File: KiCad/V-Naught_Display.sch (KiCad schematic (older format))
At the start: 22 parts, among them J1 USB_B_Micro, J2 I2C Header, J3 Conn_01x03, J4 Conn_01x02, SW1 SW_SPST, SW2 SW_SPST, SW3 SW_SPST, SW4 SW_SPST, SW5 SW_SPST, U1 AP2127K-3.3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

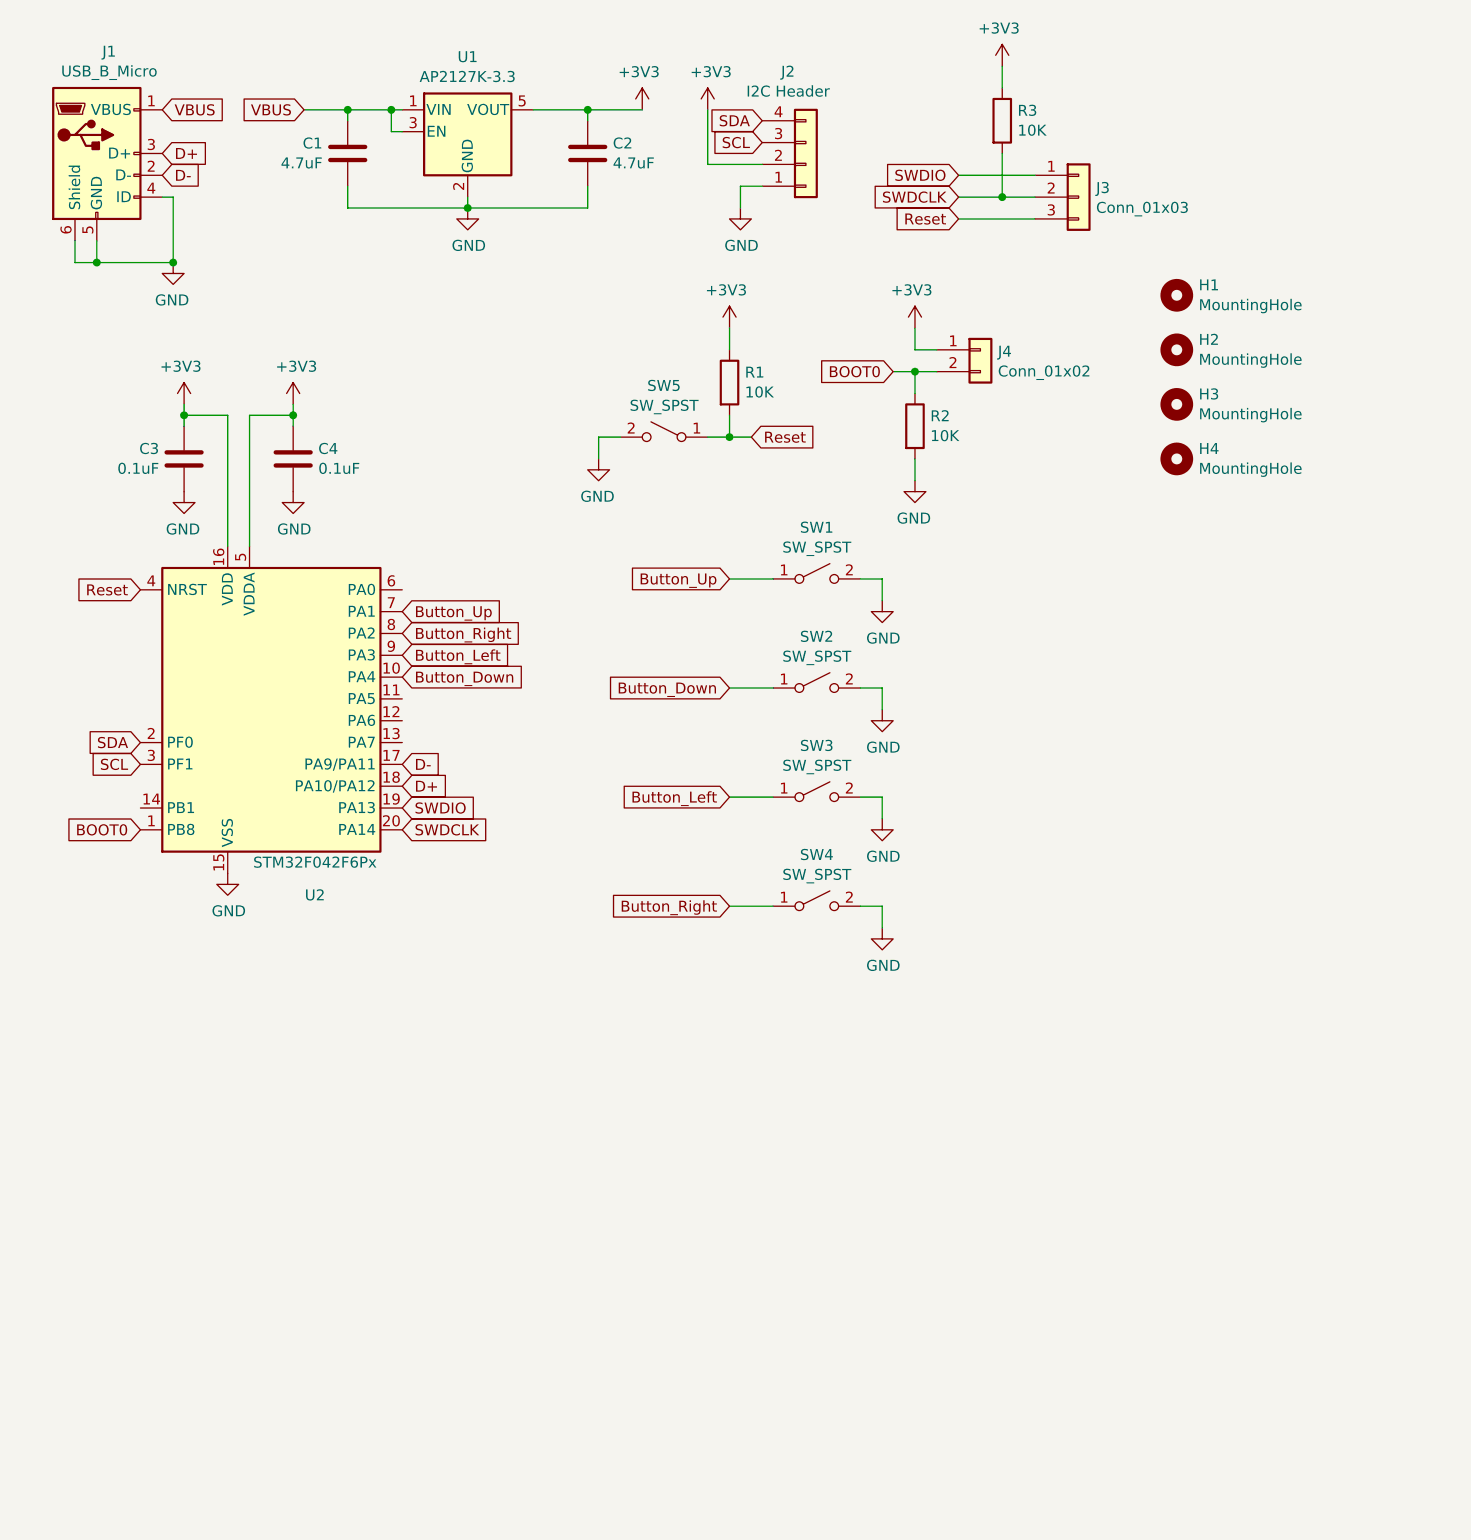
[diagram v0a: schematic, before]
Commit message: Production File updates
Added a click encoder to the center of the buttons as an additional option for input instead of discrete buttons.

Klipper Config will follow with pinmaps when the boards arrive.
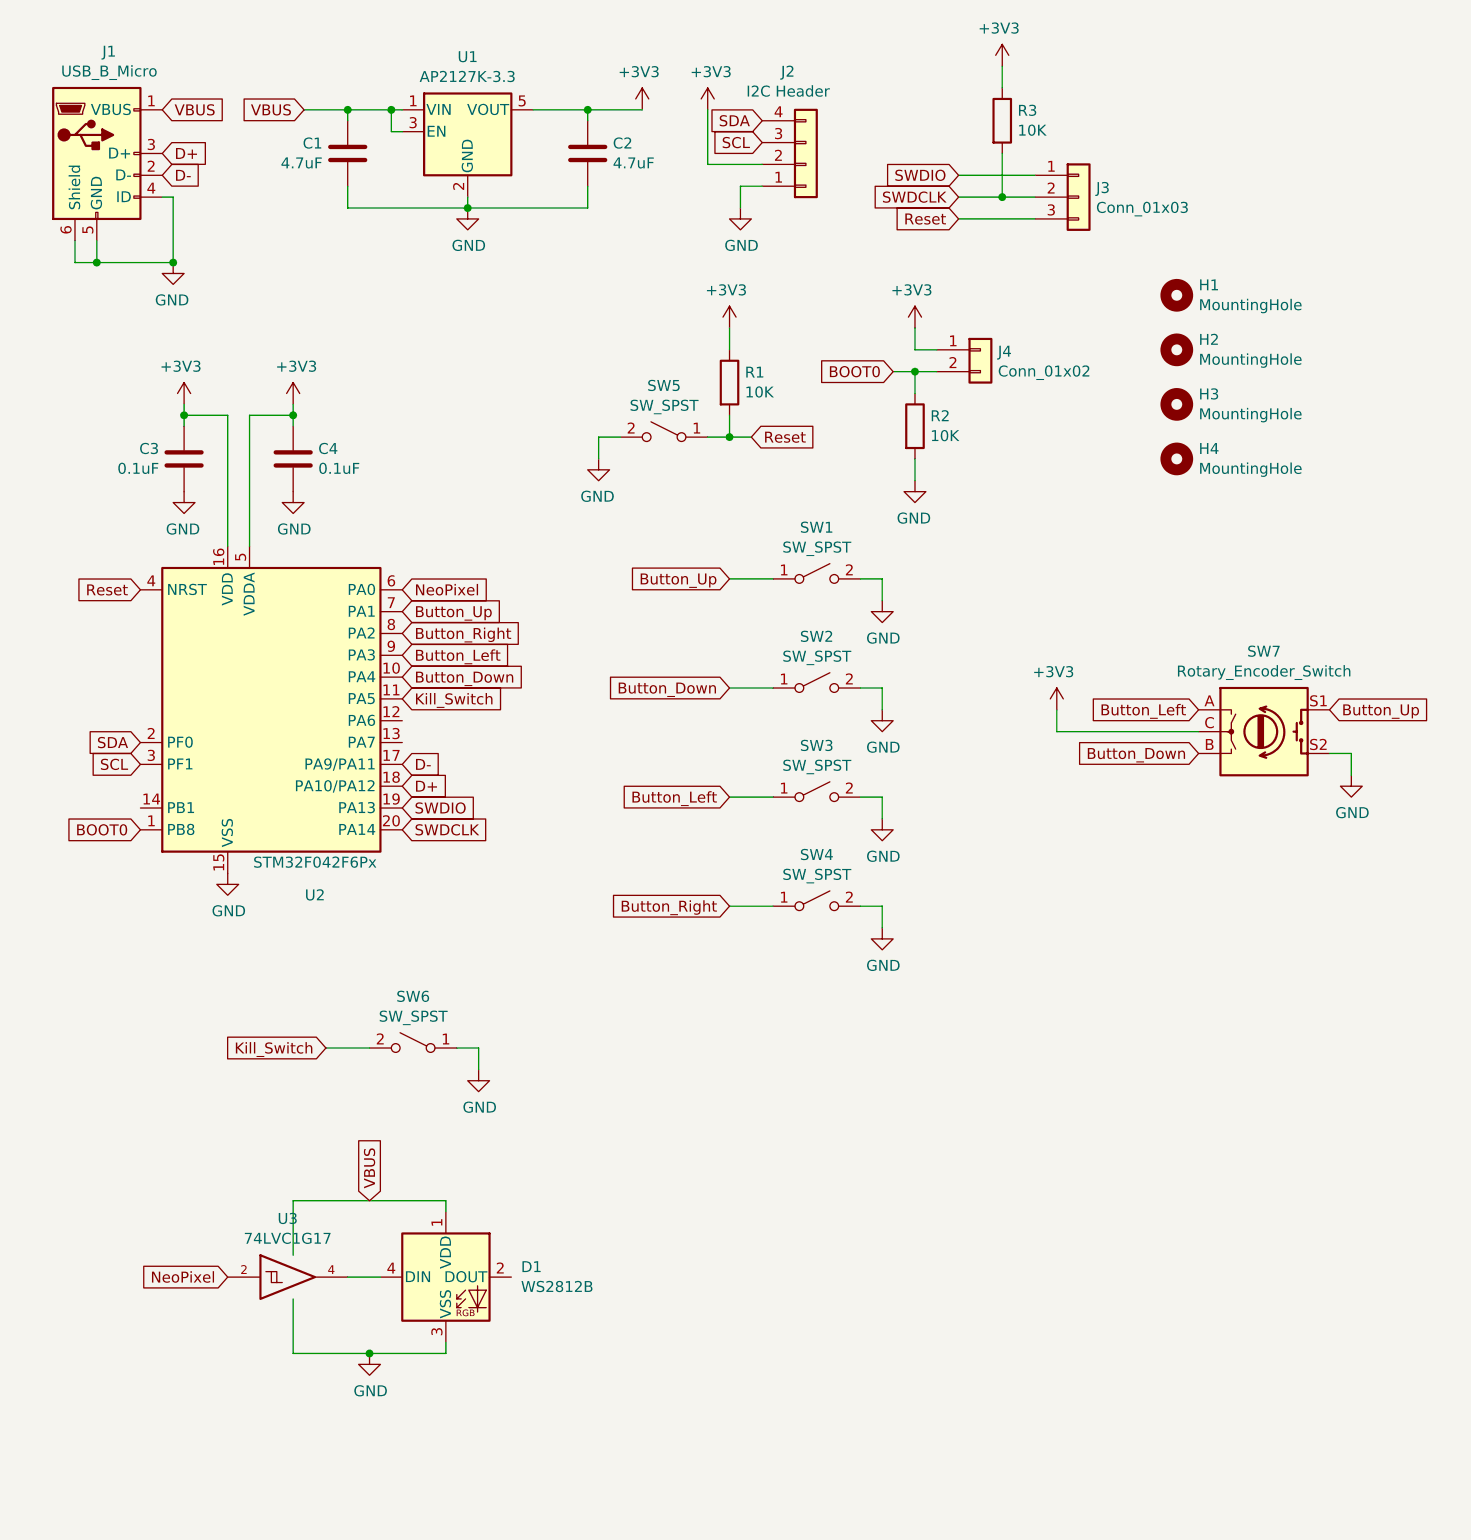
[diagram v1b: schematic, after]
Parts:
- added D1: WS2812B, LED_SMD:LED_WS2812B_PLCC4_5.0x5.0mm_P3.2mm, symbol LED:WS2812B
- added SW6: SW_SPST, Button_Switch_THT:SW_PUSH_6mm, symbol Switch:SW_SPST
- added SW7: Rotary_Encoder_Switch, TRA_KiCad_Footprints:EN11 Encoder, symbol Device:Rotary_Encoder_Switch
- added U3: 74LVC1G17, Package_TO_SOT_SMD:SOT-353_SC-70-5, symbol 74xGxx:74LVC1G17
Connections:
- net +3V3: now also SW7.C
- net Button_Down: now also SW7.B
- net Button_Left: now also SW7.A
- net Button_Up: now also SW7.S1
- net GND: now also D1.3 (VSS), SW6.1 (A), SW7.S2, U3.3 (GND)
- net Kill_Switch: now reaches U2.11 (PA5)
- net Kill_Switch: now also SW6.2 (B)
- net NeoPixel: now reaches U2.6 (PA0)
- net NeoPixel: now also U3.2
- net VBUS renamed VCC
- net VCC: now also D1.1 (VDD), U3.5 (VCC)
- new net: D1.4 (DIN), U3.4
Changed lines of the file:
@@
 	1    0    0    1
 $EndComp
+Text GLabel 1950 5250 0    50   Input ~ 0
+Kill_Switch
+$Comp
+L power:GND #PWR0120
+U 1 1 5E225054
+P 2650 5350
+F 0 "#PWR0120" H 2650 5100 50  0001 C CNN
+F 1 "GND" H 2655 5177 50  0000 C CNN
+F 2 "" H 2650 5350 50  0001 C CNN
+F 3 "" H 2650 5350 50  0001 C CNN
+	1    2650 5350
+	1    0    0    -1
+$EndComp
+Wire Wire Line
+	2650 5350 2650 5250
+Wire Wire Line
+	2650 5250 2550 5250
+Wire Wire Line
+	2150 5250 1950 5250
+Text GLabel 2300 3650 2    50   Input ~ 0
+Kill_Switch
+$Comp
+L 74xGxx:74LVC1G17 U3
+U 1 1 5E22767C
+P 1800 6300
+F 0 "U3" H 1775 6567 50  0000 C CNN
+F 1 "74LVC1G17" H 1775 6476 50  0000 C CNN
+F 2 "Package_TO_SOT_SMD:SOT-353_SC-70-5" H 1800 6300 50  0001 C CNN
+F 3 "http://www.ti.com/lit/sg/scyt129e/scyt129e.pdf" H 1800 6300 50  0001 C CNN
+	1    1800 6300
+	1    0    0    -1
+$EndComp
+Text GLabel 2150 5950 1    50   Input ~ 0
+VBUS
+$Comp
+L LED:WS2812B D1
+U 1 1 5E22982F
+P 2500 6300
+F 0 "D1" H 2844 6346 50  0000 L CNN
+F 1 "WS2812B" H 2844 6255 50  0000 L CNN
+F 2 "LED_SMD:LED_WS2812B_PLCC4_5.0x5.0mm_P3.2mm" H 2550 6000 50  0001 L TNN
+F 3 "https://cdn-shop.adafruit.com/datasheets/WS2812B.pdf" H 2600 5925 50  0001 L TNN
+	1    2500 6300
+	1    0    0    -1
+$EndComp
+Wire Wire Line
+	2500 6000 2500 5950
+Wire Wire Line
+	2500 5950 1800 5950
+Wire Wire Line
+	1800 5950 1800 6200
+Wire Wire Line
+	1800 6400 1800 6650
+Wire Wire Line
+	1800 6650 2150 6650
+Wire Wire Line
+	2500 6650 2500 6600
+Wire Wire Line
+	2200 6300 2050 6300
+$Comp
+L power:GND #PWR0121
+U 1 1 5E23384D
+P 2150 6650
+F 0 "#PWR0121" H 2150 6400 50  0001 C CNN
+F 1 "GND" H 2155 6477 50  0000 C CNN
+F 2 "" H 2150 6650 50  0001 C CNN
+F 3 "" H 2150 6650 50  0001 C CNN
+	1    2150 6650
+	1    0    0    -1
+$EndComp
+Text GLabel 1500 6300 0    50   Input ~ 0
+NeoPixel
+Text GLabel 2300 3150 2    50   Input ~ 0
+NeoPixel
+Connection ~ 2150 6650
+Wire Wire Line
+	2150 6650 2500 6650
+$Comp
+L Device:Rotary_Encoder_Switch SW7
+U 1 1 5E23C835
+P 6250 3800
+F 0 "SW7" H 6250 4167 50  0000 C CNN
+F 1 "Rotary_Encoder_Switch" H 6250 4076 50  0000 C CNN
+F 2 "TRA_KiCad_Footprints:EN11 Encoder" H 6100 3960 50  0001 C CNN
+F 3 "~" H 6250 4060 50  0001 C CNN
+	1    6250 3800
+	1    0    0    -1
+$EndComp
+Text GLabel 6550 3700 2    50   Input ~ 0
+Button_Up
+Text GLabel 5950 3900 0    50   Input ~ 0
+Button_Down
+Text GLabel 5950 3700 0    50   Input ~ 0
+Button_Left
+$Comp
+L power:GND #PWR0122
+U 1 1 5E2449F3
+P 6650 4000
+F 0 "#PWR0122" H 6650 3750 50  0001 C CNN
+F 1 "GND" H 6655 3827 50  0000 C CNN
+F 2 "" H 6650 4000 50  0001 C CNN
+F 3 "" H 6650 4000 50  0001 C CNN
+	1    6650 4000
+	1    0    0    -1
+$EndComp
+Wire Wire Line
+	6650 4000 6650 3900
+Wire Wire Line
+	6650 3900 6550 3900
+Wire Wire Line
+	5950 3800 5300 3800
+Wire Wire Line
+	5300 3800 5300 3700
+$Comp
+L power:+3V3 #PWR0123
+U 1 1 5E248221
+P 5300 3700
+F 0 "#PWR0123" H 5300 3550 50  0001 C CNN
+F 1 "+3V3" H 5315 3873 50  0000 C CNN
+F 2 "" H 5300 3700 50  0001 C CNN
+F 3 "" H 5300 3700 50  0001 C CNN
+	1    5300 3700
+	-1   0    0    -1
+$EndComp
+$Comp
+L Switch:SW_SPST SW6
+U 1 1 5E24B6BA
+P 2350 5250
+F 0 "SW6" H 2350 5485 50  0000 C CNN
+F 1 "SW_SPST" H 2350 5394 50  0000 C CNN
+F 2 "Button_Switch_THT:SW_PUSH_6mm" H 2350 5250 50  0001 C CNN
+F 3 "~" H 2350 5250 50  0001 C CNN
+	1    2350 5250
+	-1   0    0    -1
+$EndComp
 $EndSCHEMATC

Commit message: Second I2C Header
Added a second I2C header for baords with reversed Vcc and Gnd pins.
Also added a full SWD header as well

Updated Production files
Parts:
- added J5: SWD Header, Connector_PinHeader_1.27mm:PinHeader_2x05_P1.27mm_Vertical_SMD, symbol Connector_Generic:Conn_02x05_Odd_Even
- added J6: I2C Header 2, Connector_PinHeader_2.54mm:PinHeader_1x04_P2.54mm_Vertical, symbol Connector_Generic:Conn_01x04
- J2: value I2C Header -> I2C Header 1
- U3: LCSC (none) -> C124293
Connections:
- net +3V3: now also J5.1 (Pin_1), J6.1 (Pin_1)
- net GND: now also J5.3 (Pin_3), J5.5 (Pin_5), J6.2 (Pin_2)
- net SCL: now also J6.3 (Pin_3)
- net SDA: now also J6.4 (Pin_4)
- net SWDCLK: now also J5.4 (Pin_4)
- net SWDIO: now also J5.2 (Pin_2)
- net Reset renamed ~Reset
- net ~Reset: now also J5.10 (Pin_10)
- no-connect marks 0 -> 4
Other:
- moved on the sheet: J3, R3
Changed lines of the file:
@@
 $EndComp
 Text GLabel 1100 3150 0    50   Input ~ 0
-Reset
+~Reset
 Text GLabel 1100 3850 0    50   Input ~ 0
 SDA
@@
 L Connector_Generic:Conn_01x03 J3
 U 1 1 5E2313D9
-P 5400 1350
-F 0 "J3" H 5480 1392 50  0000 L CNN
-F 1 "Conn_01x03" H 5480 1301 50  0000 L CNN
-F 2 "Connector_PinHeader_2.54mm:PinHeader_1x03_P2.54mm_Vertical" H 5400 1350 50  0001 C CNN
-F 3 "~" H 5400 1350 50  0001 C CNN
-	1    5400 1350
+P 6150 1350
+F 0 "J3" H 6230 1392 50  0000 L CNN
+F 1 "Conn_01x03" H 6230 1301 50  0000 L CNN
+F 2 "Connector_PinHeader_2.54mm:PinHeader_1x03_P2.54mm_Vertical" H 6150 1350 50  0001 C CNN
+F 3 "~" H 6150 1350 50  0001 C CNN
+	1    6150 1350
 	1    0    0    -1
 $EndComp
@@
 Text GLabel 2300 4250 2    50   Input ~ 0
 SWDCLK
-Text GLabel 4850 1250 0    50   Input ~ 0
+Text GLabel 5600 1250 0    50   Input ~ 0
 SWDIO
-Text GLabel 4850 1350 0    50   Input ~ 0
+Text GLabel 5600 1350 0    50   Input ~ 0
 SWDCLK
-Text GLabel 3900 2450 2    50   Input ~ 0
-Reset
-Text GLabel 4850 1450 0    50   Input ~ 0
-Reset
-Wire Wire Line
-	5200 1450 4850 1450
-Wire Wire Line
-	4850 1350 5050 1350
-Wire Wire Line
-	5200 1250 4850 1250
-Wire Wire Line
-	5050 1350 5050 1150
-Connection ~ 5050 1350
-Wire Wire Line
-	5050 1350 5200 1350
+Wire Wire Line
+	5950 1450 5600 1450
+Wire Wire Line
+	5600 1350 5800 1350
+Wire Wire Line
+	5950 1250 5600 1250
+Wire Wire Line
+	5800 1350 5800 1150
+Connection ~ 5800 1350
+Wire Wire Line
+	5800 1350 5950 1350
 $Comp
 L Device:R R3
 U 1 1 5E2437B3
-P 5050 1000
-F 0 "R3" H 5120 1046 50  0000 L CNN
-F 1 "10K" H 5120 955 50  0000 L CNN
-F 2 "Resistor_SMD:R_0805_2012Metric" V 4980 1000 50  0001 C CNN
-F 3 "~" H 5050 1000 50  0001 C CNN
-F 4 "C17414" H 5050 1000 50  0001 C CNN "LCSC"
-	1    5050 1000
-	1    0    0    -1
-$EndComp
-Wire Wire Line
-	5050 850  5050 750
+P 5800 1000
+F 0 "R3" H 5870 1046 50  0000 L CNN
+F 1 "10K" H 5870 955 50  0000 L CNN
+F 2 "Resistor_SMD:R_0805_2012Metric" V 5730 1000 50  0001 C CNN
+F 3 "~" H 5800 1000 50  0001 C CNN
+F 4 "C17414" H 5800 1000 50  0001 C CNN "LCSC"
+	1    5800 1000
+	1    0    0    -1
+$EndComp
+Wire Wire Line
+	5800 850  5800 750
 $Comp
 L power:+3V3 #PWR0119
 U 1 1 5E2437BA
-P 5050 750
-F 0 "#PWR0119" H 5050 600 50  0001 C CNN
-F 1 "+3V3" H 5065 923 50  0000 C CNN
-F 2 "" H 5050 750 50  0001 C CNN
-F 3 "" H 5050 750 50  0001 C CNN
-	1    5050 750
+P 5800 750
+F 0 "#PWR0119" H 5800 600 50  0001 C CNN
+F 1 "+3V3" H 5815 923 50  0000 C CNN
+F 2 "" H 5800 750 50  0001 C CNN
+F 3 "" H 5800 750 50  0001 C CNN
+	1    5800 750
 	-1   0    0    -1
 $EndComp
@@
 P 4150 1200
 F 0 "J2" H 4068 775 50  0000 C CNN
-F 1 "I2C Header" H 4068 866 50  0000 C CNN
+F 1 "I2C Header 1" H 4068 866 50  0000 C CNN
 F 2 "TRA_KiCad_Footprints:1pt3in_OLED" H 4150 1200 50  0001 C CNN
 F 3 "~" H 4150 1200 50  0001 C CNN
@@
 F 2 "Package_TO_SOT_SMD:SOT-353_SC-70-5" H 1800 6300 50  0001 C CNN
 F 3 "http://www.ti.com/lit/sg/scyt129e/scyt129e.pdf" H 1800 6300 50  0001 C CNN
+F 4 "C124293" H 1800 6300 50  0001 C CNN "LCSC"
 	1    1800 6300
 	1    0    0    -1
@@
 	-1   0    0    -1
 $EndComp
+$Comp
+L Connector_Generic:Conn_02x05_Odd_Even J5
+U 1 1 5E2B51F8
+P 4500 6000
+F 0 "J5" H 4550 6417 50  0000 C CNN
+F 1 "SWD Header" H 4550 6326 50  0000 C CNN
+F 2 "Connector_PinHeader_1.27mm:PinHeader_2x05_P1.27mm_Vertical_SMD" H 4500 6000 50  0001 C CNN
+F 3 "~" H 4500 6000 50  0001 C CNN
+	1    4500 6000
+	1    0    0    -1
+$EndComp
+Wire Wire Line
+	4300 5900 4100 5900
+Wire Wire Line
+	4100 5900 4100 6000
+Wire Wire Line
+	4300 6000 4100 6000
+Connection ~ 4100 6000
+Wire Wire Line
+	4100 6000 4100 6200
+Wire Wire Line
+	4300 5800 4100 5800
+Wire Wire Line
+	4100 5800 4100 5650
+$Comp
+L power:GND #PWR0124
+U 1 1 5E2BBF7F
+P 4100 6200
+F 0 "#PWR0124" H 4100 5950 50  0001 C CNN
+F 1 "GND" H 4105 6027 50  0000 C CNN
+F 2 "" H 4100 6200 50  0001 C CNN
+F 3 "" H 4100 6200 50  0001 C CNN
+	1    4100 6200
+	1    0    0    -1
+$EndComp
+$Comp
+L power:+3V3 #PWR0125
+U 1 1 5E2BDDEA
+P 4100 5650
+F 0 "#PWR0125" H 4100 5500 50  0001 C CNN
+F 1 "+3V3" H 4115 5823 50  0000 C CNN
+F 2 "" H 4100 5650 50  0001 C CNN
+F 3 "" H 4100 5650 50  0001 C CNN
+	1    4100 5650
+	1    0    0    -1
+$EndComp
+Text GLabel 4900 5800 2    50   Input ~ 0
+SWDIO
+Text GLabel 4900 5900 2    50   Input ~ 0
+SWDCLK
+Text GLabel 3900 2450 2    50   Input ~ 0
+~Reset
+Text GLabel 5600 1450 0    50   Input ~ 0
+~Reset
+Text GLabel 4900 6200 2    50   Input ~ 0
+~Reset
+Wire Wire Line
+	4900 5800 4800 5800
+Wire Wire Line
+	4800 5900 4900 5900
+Wire Wire Line
+	4900 6200 4800 6200
+NoConn ~ 4800 6100
+NoConn ~ 4800 6000
+NoConn ~ 4300 6100
+NoConn ~ 4300 6200
+$Comp
+L power:+3V3 #PWR0126
+U 1 1 5E2ECBBA
+P 4500 950
+F 0 "#PWR0126" H 4500 800 50  0001 C CNN
+F 1 "+3V3" H 4515 1123 50  0000 C CNN
+F 2 "" H 4500 950 50  0001 C CNN
+F 3 "" H 4500 950 50  0001 C CNN
+	1    4500 950
+	1    0    0    -1
+$EndComp
+$Comp
+L power:GND #PWR0127
+U 1 1 5E2ECBC0
+P 4600 1400
+F 0 "#PWR0127" H 4600 1150 50  0001 C CNN
+F 1 "GND" H 4605 1227 50  0000 C CNN
+F 2 "" H 4600 1400 50  0001 C CNN
+F 3 "" H 4600 1400 50  0001 C CNN
+	1    4600 1400
+	1    0    0    -1
+$EndComp
+Text GLabel 4750 1000 0    50   Input ~ 0
+SDA
+Text GLabel 4750 1100 0    50   Input ~ 0
+SCL
+$Comp
+L Connector_Generic:Conn_01x04 J6
+U 1 1 5E2ECBCC
+P 4950 1200
+F 0 "J6" H 4868 775 50  0000 C CNN
+F 1 "I2C Header 2" H 4868 866 50  0000 C CNN
+F 2 "Connector_PinHeader_2.54mm:PinHeader_1x04_P2.54mm_Vertical" H 4950 1200 50  0001 C CNN
+F 3 "~" H 4950 1200 50  0001 C CNN
+	1    4950 1200
+	1    0    0    1
+$EndComp
+Wire Wire Line
+	4750 1300 4500 1300
+Wire Wire Line
+	4500 950  4500 1300
+Wire Wire Line
+	4750 1200 4600 1200
+Wire Wire Line
+	4600 1200 4600 1400
 $EndSCHEMATC
